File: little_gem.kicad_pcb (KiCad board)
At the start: 2 copper layers, 31.2 x 18.6 mm, 11 parts, among them J1 AudioPlug2, U1 LM386

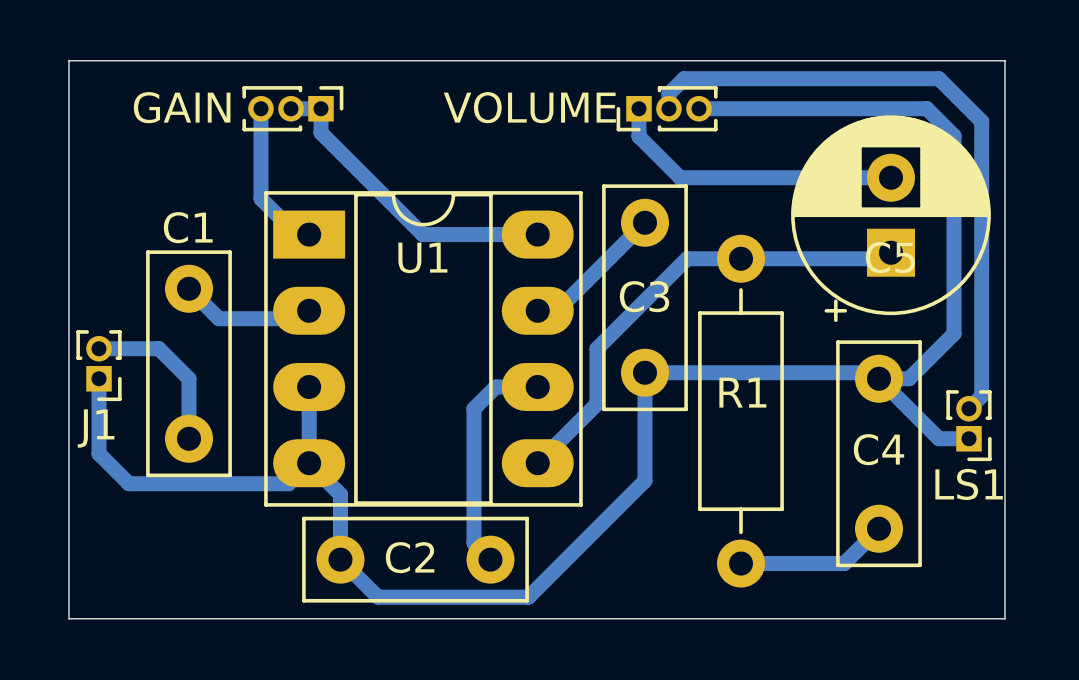
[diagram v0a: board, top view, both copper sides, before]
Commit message: replaced footprints for pots and connectors
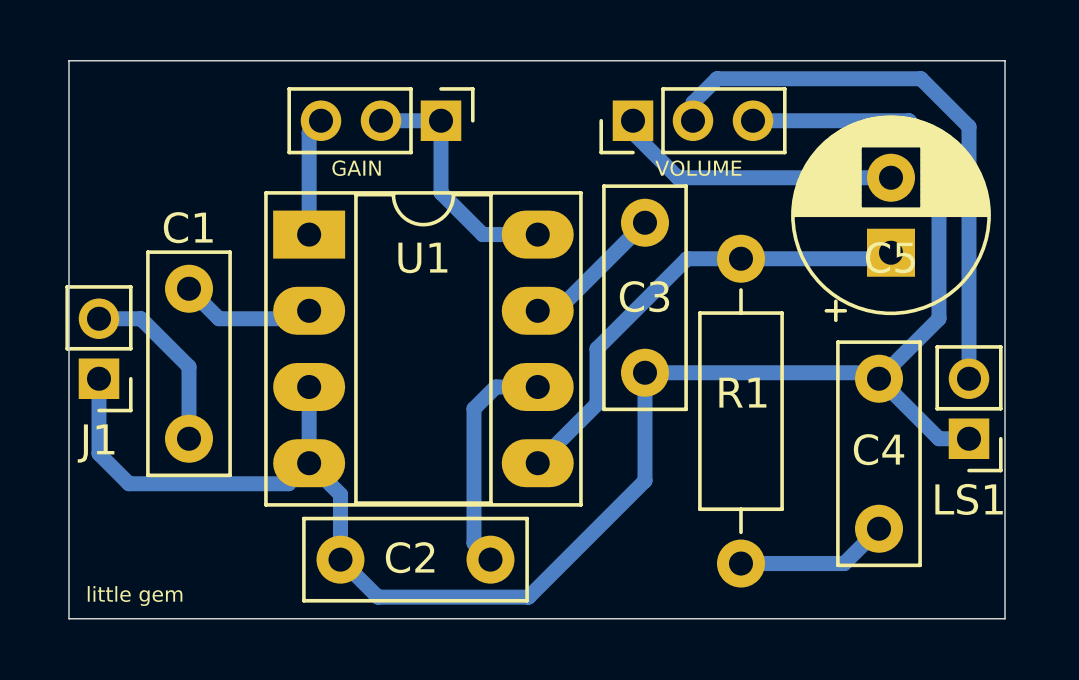
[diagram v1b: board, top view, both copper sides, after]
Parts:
- removed the GAIN at (140.4, 98.0)
- removed the VOLUME at (151.0, 98.0)
- added GAIN: 5k, Connector_PinHeader_2.00mm:PinHeader_1x03_P2.00mm_Vertical, F.Cu at (144.4, 98.4)
- added VOLUME: 25, Connector_PinHeader_2.00mm:PinHeader_1x03_P2.00mm_Vertical, F.Cu at (150.8, 98.4)
- J1: footprint Connector_PinHeader_1.00mm:PinHeader_1x02_P1.00mm_Vertical_audio_jack -> Connector_PinHeader_2.00mm:PinHeader_1x02_P2.00mm_Vertical_LittleGem
- LS1: footprint Connector_PinHeader_1.00mm:PinHeader_1x02_P1.00mm_Vertical -> Connector_PinHeader_2.00mm:PinHeader_1x02_P2.00mm_Vertical
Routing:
- net GND: track 62.6 -> 59.0 mm
- net Net-(LS1-Pad2): track 21.5 -> 19.2 mm
- net Net-(GAIN1-Pad1): track 10.4 -> 8.20 mm
- net Net-(GAIN1-Pad3): track 5.10 -> 3.96 mm
- net Net-(C1-Pad2): track 5.41 -> 6.06 mm
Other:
- board text added: "little gem"

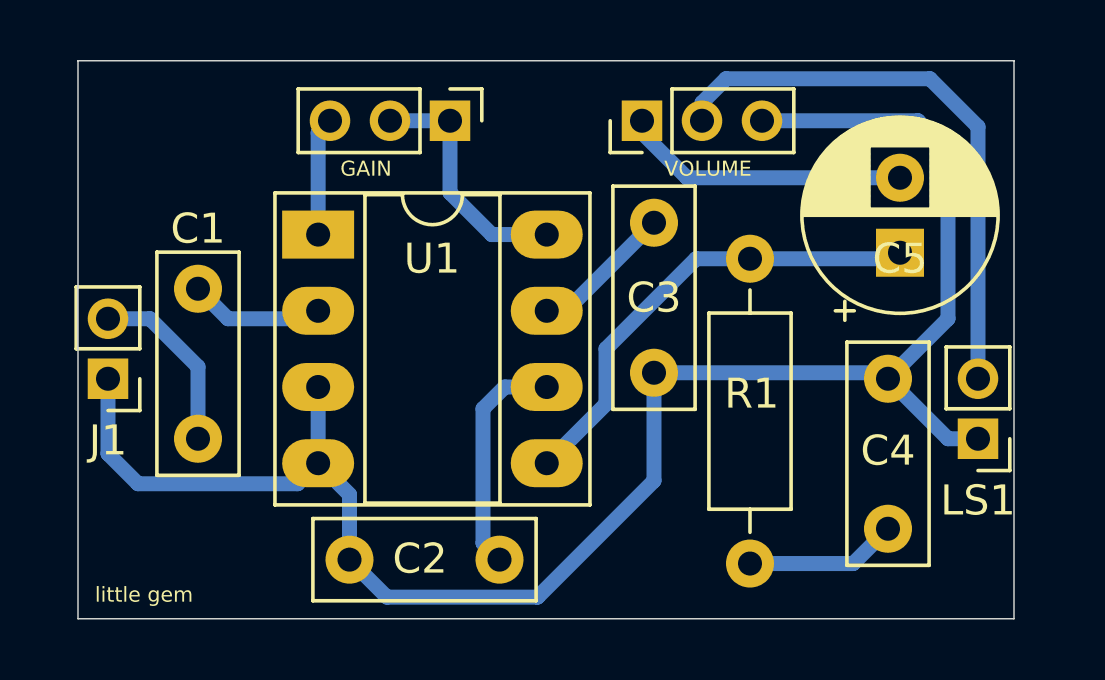
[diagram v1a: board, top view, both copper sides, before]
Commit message: added mounting holes
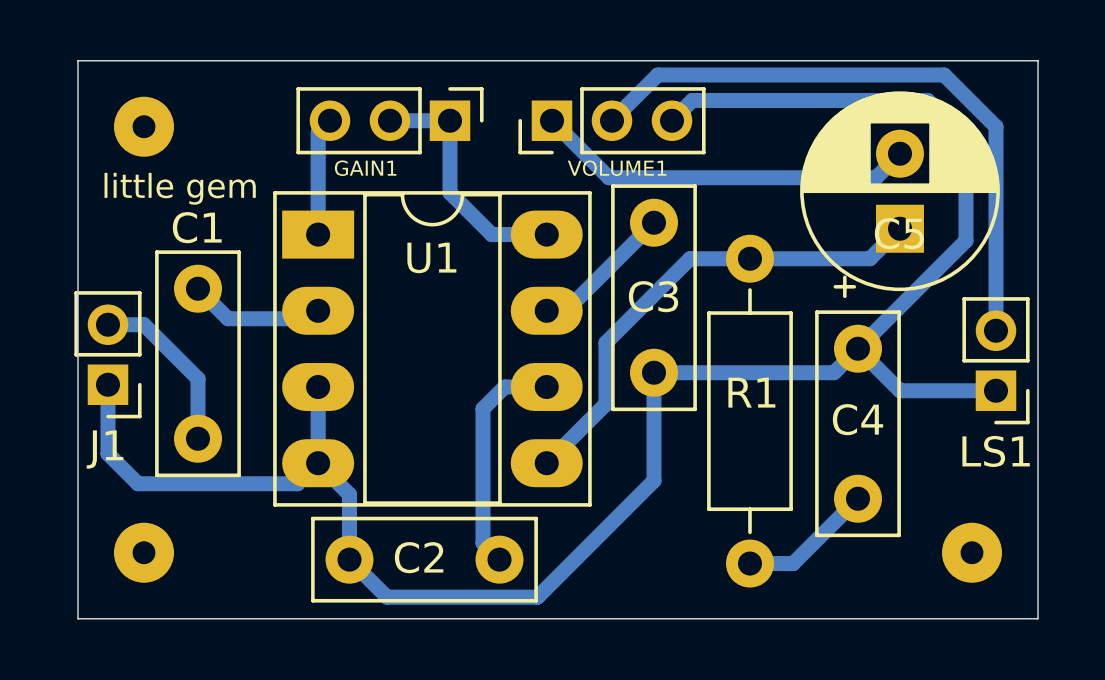
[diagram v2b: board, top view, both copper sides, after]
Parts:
- added MNT: mount_hole_3mm, MountingHole:mount_hole_3mm, F.Cu at (134.2, 98.6)
- added MNT: mount_hole_3mm, MountingHole:mount_hole_3mm, F.Cu at (134.2, 112.8)
- added MNT: mount_hole_3mm, MountingHole:mount_hole_3mm, F.Cu at (161.8, 112.8)
- moved VOLUME1 3.00 mm to (147.8, 98.4)
- moved LS1 1.71 mm to (162.6, 107.4)
- moved C4 1.41 mm to (158.0, 111.0)
- moved C5 0.80 mm to (159.4, 102.0)
- moved J1 0.20 mm to (133.0, 107.2)
- renumbered GAIN to GAIN1, VOLUME to VOLUME1
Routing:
- net GND: track 59.0 -> 63.8 mm
- net Net-(C5-Pad2): track 9.62 -> 12.7 mm
- net Net-(LS1-Pad2): track 19.2 -> 20.9 mm
- net Net-(C4-Pad1): track 5.08 -> 4.49 mm
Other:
- board size 31.2 x 18.6 mm -> 32 x 18.6 mm

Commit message: added PCB name
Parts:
- moved C2 5.15 mm to (151.2, 113.0)
- renumbered GAIN1 to GAIN, VOLUME1 to VOLUME
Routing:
- net +9V: track 7.68 -> 12.8 mm
- net GND: track 63.8 -> 66.7 mm
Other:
- board text added: "little_gem v1.0"
- board text removed: "little gem"

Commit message: added JLC order number location
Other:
- board text added: "JLCJLCJLCJLC"
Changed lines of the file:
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@@
   (general
     (thickness 1.6)
-    (drawings 6)
+    (drawings 7)
     (tracks 60)
     (zones 0)
@@
   (page A4)
   (layers
-    (0 F.Cu signal)
-    (31 B.Cu signal)
+    (0 F.Cu signal hide)
+    (31 B.Cu signal hide)
     (32 B.Adhes user hide)
     (33 F.Adhes user hide)
@@
     (visible_elements FFFFFF7F)
     (pcbplotparams
-      (layerselection 0x010fc_ffffffff)
+      (layerselection 0x010f0_ffffffff)
       (usegerberextensions false)
-      (usegerberattributes true)
-      (usegerberadvancedattributes true)
-      (creategerberjobfile true)
+      (usegerberattributes false)
+      (usegerberadvancedattributes false)
+      (creategerberjobfile false)
       (excludeedgelayer true)
       (linewidth 0.100000)
@@
       (psa4output false)
       (plotreference true)
-      (plotvalue true)
+      (plotvalue false)
       (plotinvisibletext false)
-      (padsonsilk false)
+      (padsonsilk true)
       (subtractmaskfromsilk false)
-      (outputformat 4)
+      (outputformat 1)
       (mirror false)
       (drillshape 0)
       (scaleselection 1)
-      (outputdirectory "./"))
+      (outputdirectory "./gerber/"))
   )
   (net 0 "")
@@
     )
   )
+  (gr_text JLCJLCJLCJLC (at 145.2 108.6 90) (layer F.SilkS)
+    (effects (font (size 0.85 0.4) (thickness 0.1)))
+  )
   (gr_text "little_gem \nv1.0" (at 140.2 113.2) (layer F.SilkS)

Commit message: added power pins
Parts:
- removed MNT (x3): mount_hole_3mm, MountingHole:mount_hole_3mm
- added J2: Conn_01x02_Female, Connector_PinHeader_2.54mm:PinHeader_2x01_P2.54mm_Vertical, F.Cu at (145.0, 90.4)
- renumbered GAIN to GAIN1, VOLUME to VOLUME1

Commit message: Fixed footprints
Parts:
- removed GAIN1: 5k, Connector_PinHeader_2.00mm:PinHeader_1x03_P2.00mm_Vertical
- removed VOLUME1: 25, Connector_PinHeader_2.00mm:PinHeader_1x03_P2.00mm_Vertical
- added GAIN: 5k, Connector_PinHeader_2.54mm:PinHeader_1x03_P2.54mm_Vertical, F.Cu at (146.2, 97.0)
- added VOLUME: 25, Connector_PinHeader_2.54mm:PinHeader_1x03_P2.54mm_Vertical, F.Cu at (149.8, 97.0)
- J1: value AudioPlug2 -> Conn_01x02_Female; footprint Connector_PinHeader_2.00mm:PinHeader_1x02_P2.00mm_Vertical_LittleGem -> Connector_PinHeader_2.54mm:PinHeader_1x02_P2.54mm_Vertical
- LS1: footprint Connector_PinHeader_2.00mm:PinHeader_1x02_P2.00mm_Vertical -> Connector_PinHeader_2.54mm:PinHeader_1x02_P2.54mm_Vertical
- moved J2 12.0 mm to (135.0, 97.0)
- moved C2 2.80 mm to (148.4, 112.9)
- moved J1 1.53 mm to (133.3, 105.7), turned to 0 degrees
- moved LS1 0.80 mm to (162.6, 108.2)
- moved C1 0.60 mm to (136.6, 104.0)
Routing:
- net Net-(GAIN1-Pad3): track 3.96 -> 20.7 mm
- net +9V: track 12.8 -> 25.9 mm
- net GND: track 66.7 -> 76.2 mm
- net Net-(LS1-Pad2): track 20.9 -> 18.5 mm
- net Net-(C1-Pad2): track 5.75 -> 3.61 mm
- net Net-(C5-Pad2): track 12.7 -> 11.4 mm
- net Net-(C1-Pad1): track 4.53 -> 3.71 mm
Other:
- board size 32 x 18.6 mm -> 32 x 20 mm

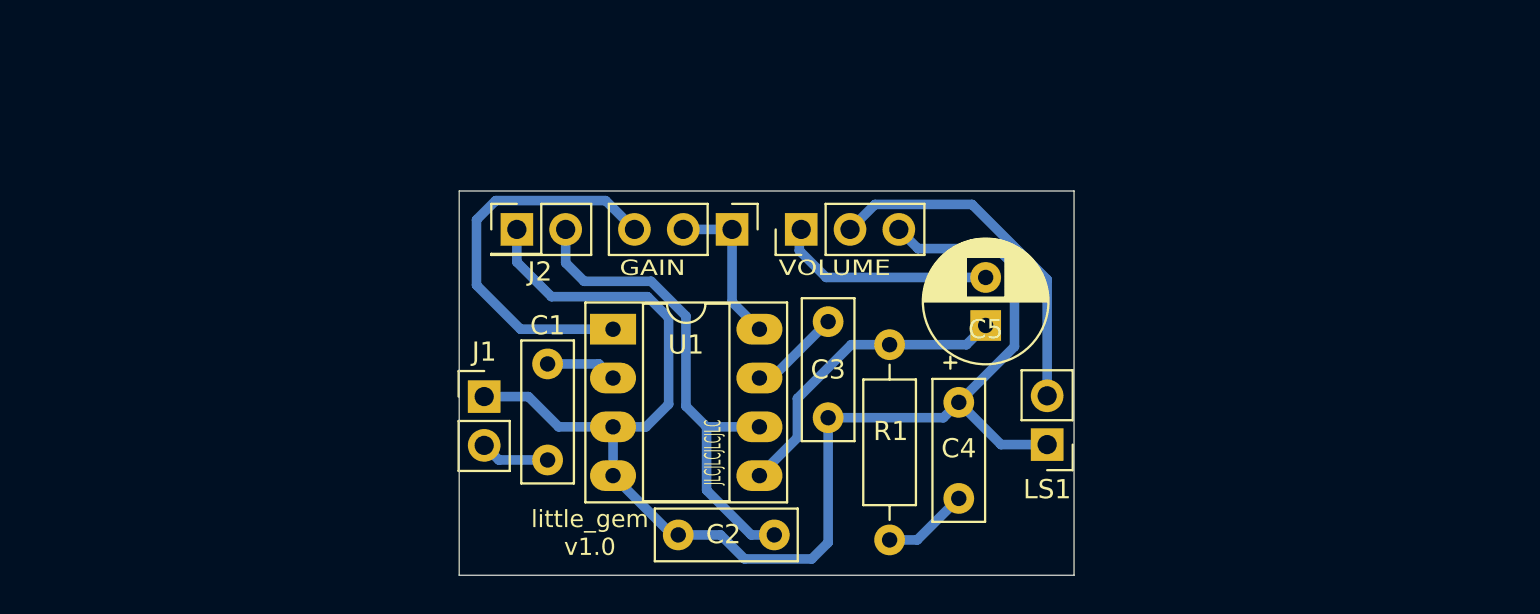
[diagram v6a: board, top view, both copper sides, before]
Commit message: added led
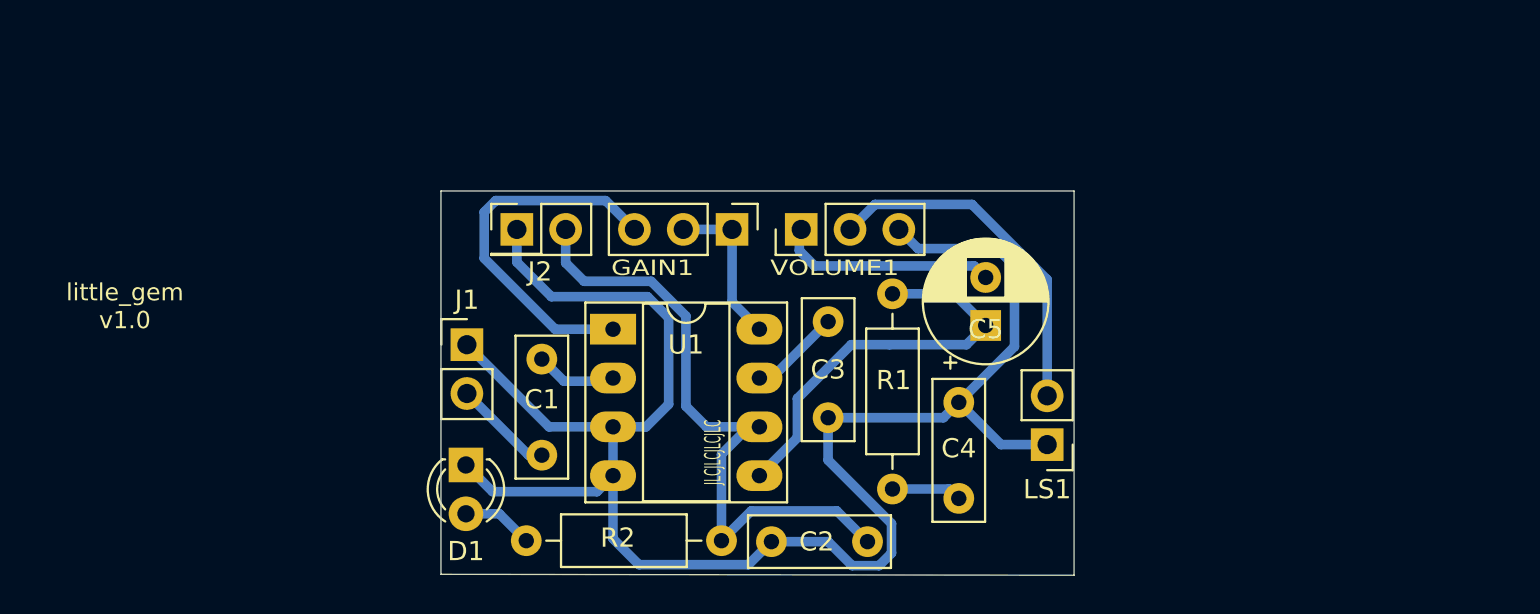
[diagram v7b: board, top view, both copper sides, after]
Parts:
- added D1: LED, LED_THT:LED_D3.0mm, F.Cu at (132.3, 109.3)
- added R2: 2K2, Resistor_THT:R_Axial_DIN0207_L6.3mm_D2.5mm_P10.16mm_Horizontal, F.Cu at (145.7, 113.2)
- moved C2 4.86 mm to (153.2, 113.2)
- moved J1 2.85 mm to (132.4, 103.0)
- moved R1 2.65 mm to (154.6, 100.3)
- moved C1 0.39 mm to (136.3, 103.8)
- renumbered GAIN to GAIN1, VOLUME to VOLUME1
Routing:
- net GND: track 76.2 -> 95.0 mm
- net +9V: track 25.9 -> 34.1 mm
- net Net-(C5-Pad1): track 16.2 -> 21.7 mm
- net Net-(D1-Pad2): track 0.00 -> 3.72 mm
- net Net-(C1-Pad2): track 3.61 -> 5.23 mm
- net Net-(GAIN1-Pad3): track 20.7 -> 19.3 mm
- net Net-(C4-Pad1): track 4.49 -> 3.65 mm
- net Net-(C1-Pad1): track 3.71 -> 4.25 mm
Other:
- board size 32 x 20 mm -> 32.9 x 20 mm

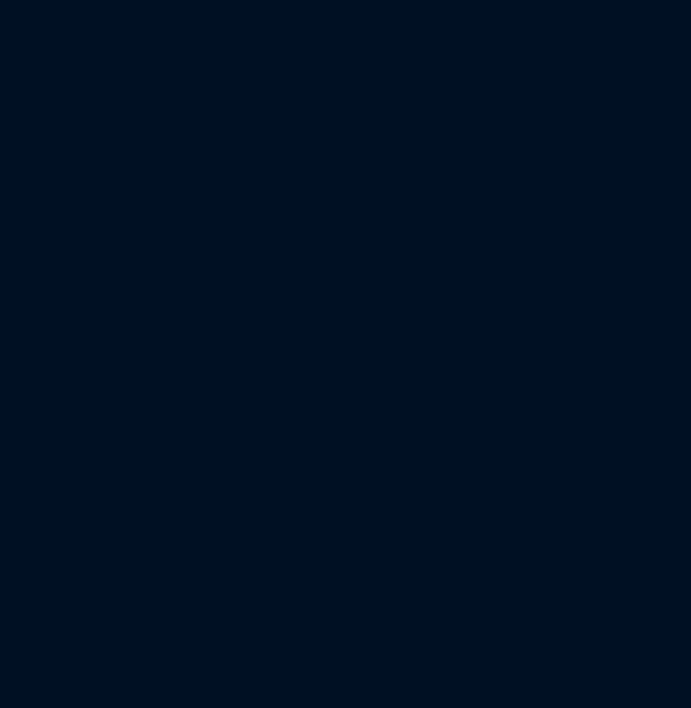
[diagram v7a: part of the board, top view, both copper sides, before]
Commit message: added 3.5mm jack
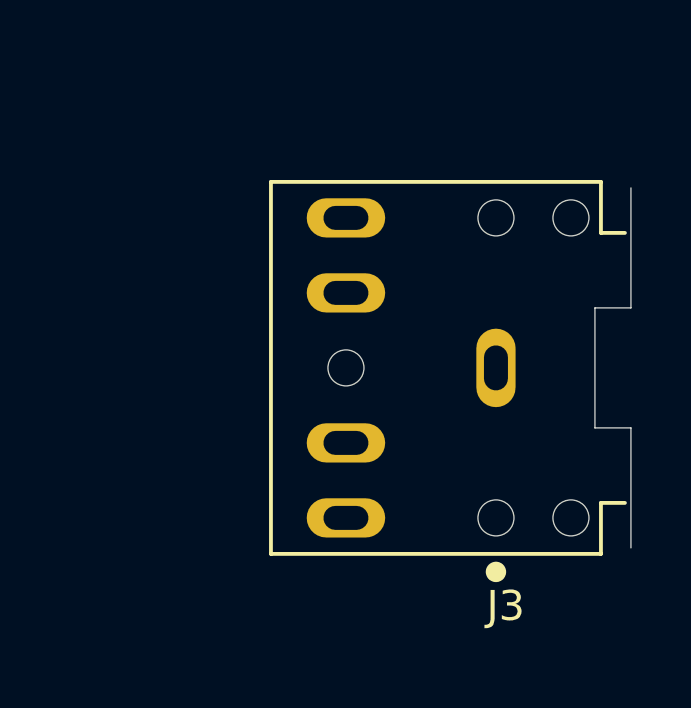
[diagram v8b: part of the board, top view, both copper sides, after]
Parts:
- added J3: SJ1-3525N, CUI_SJ1-3525N, F.Cu at (181.8, 105.7)
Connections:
- LS1 pad 2: Net-(LS1-Pad2) -> Net-(J3-Pad11)
- VOLUME1 pad 2: Net-(LS1-Pad2) -> Net-(J3-Pad2)
